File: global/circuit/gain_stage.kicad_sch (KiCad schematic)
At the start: 10 parts, among them U3 TL081H

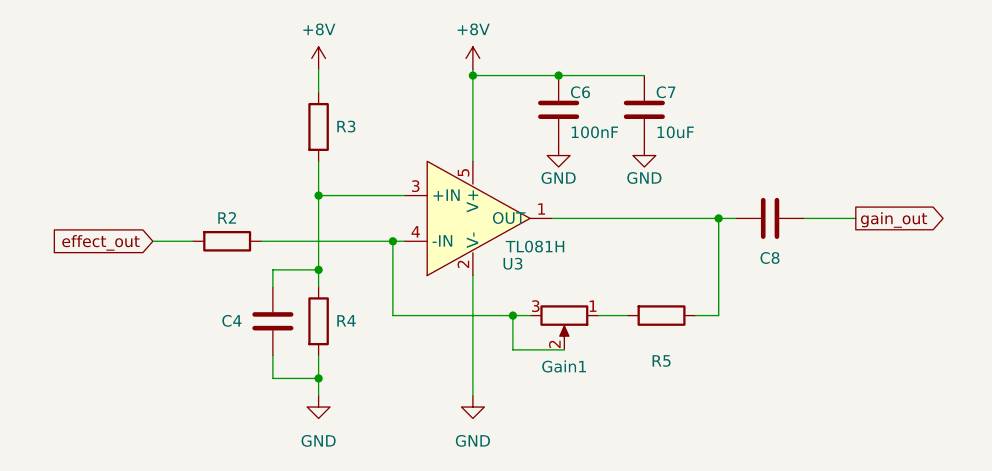
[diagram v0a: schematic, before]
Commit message: add circuit dimensioning
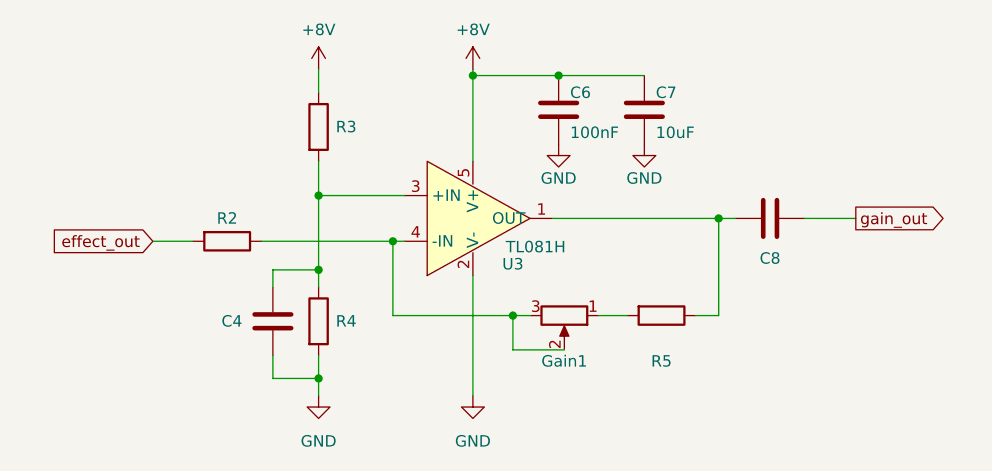
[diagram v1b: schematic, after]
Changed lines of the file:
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@@
   (symbol (lib_id "Device:R_Potentiometer") (at 111.76 64.77 270) (unit 1)
     (in_bom yes) (on_board yes)
-    (property "Reference" "Gain1" (id 0) (at 111.76 70.485 90))
+    (property "Reference" "Gain1" (id 0) (at 111.76 69.85 90))
     (property "Value" "10k" (id 1) (at 111.76 71.12 90)
       (effects (font (size 1.27 1.27)) hide)
